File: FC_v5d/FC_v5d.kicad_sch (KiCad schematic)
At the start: 73 parts, among them IC3 RV-3028-C7_32.768kHz_1ppm_TA_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, J1 Conn_01x02, J12 USB_C_Receptacle_USB2.0_16P, J16 DEBUG, J18 Payload, J22 SWD Port, J3 Life Makes Lemonade, J5 BM04B-SRSS-TB(LF)(SN), J6 Conn_Coaxial, SW1 KMR2, SW2 KMR2, U12 TCA9548ARGERQ1, U14 TCA4307DGKR, U2 ZDSD04GLGEAG, U30 E28-2G4M27S, U4 RFM98PW, U7 LSM6DSOTR, U8 LSM303AGRTR

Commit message: Added XTSD Decoupling Cap
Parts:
- added C28: 100nf, Capacitor_SMD:C_0402_1005Metric, symbol Adafruit ItsyBitsy RP2040-eagle-import:CAP_CERAMIC_0402NO
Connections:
- net +3V3: now also C28.1
- net GND: now also C28.2
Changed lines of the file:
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@@
 	)
 	(junction
+		(at 64.77 222.25)
+		(diameter 0)
+		(color 0 0 0 0)
+	)
+	(junction
 		(at 237.49 125.73)
 		(diameter 0)
@@
 	(wire
 		(pts
+			(xy 64.77 222.25) (xy 71.12 222.25)
+		)
+		(stroke
+			(width 0)
+			(type default)
+		)
+	)
+	(wire
+		(pts
 			(xy 220.98 250.19) (xy 223.52 250.19)
 		)
@@
 	(wire
 		(pts
+			(xy 64.77 222.25) (xy 64.77 236.22)
+		)
+		(stroke
+			(width 0)
+			(type default)
+		)
+	)
+	(wire
+		(pts
 			(xy 397.002 44.45) (xy 397.002 29.591)
 		)
@@
 	(wire
 		(pts
+			(xy 71.12 222.25) (xy 71.12 226.06)
+		)
+		(stroke
+			(width 0)
+			(type default)
+		)
+	)
+	(wire
+		(pts
 			(xy 27.94 238.76) (xy 31.75 238.76)
 		)
@@
 	(wire
 		(pts
-			(xy 64.77 222.25) (xy 64.77 236.22)
-		)
-		(stroke
-			(width 0)
-			(type default)
-		)
-	)
-	(wire
-		(pts
 			(xy 163.83 232.41) (xy 166.37 232.41)
 		)
@@
 	)
 	(symbol
+		(lib_id "power:GND")
+		(at 71.12 233.68 0)
+		(unit 1)
+		(exclude_from_sim no)
+		(in_bom yes)
+		(on_board yes)
+		(dnp no)
+		(fields_autoplaced yes)
+		(property "Reference" "#PWR056"
+			(at 71.12 240.03 0)
+			(effects
+				(font
+					(size 1.27 1.27)
+				)
+				(hide yes)
+			)
+		)
+		(property "Value" "GND"
+			(at 71.12 238.1234 0)
+			(effects
+				(font
+					(size 1.27 1.27)
+				)
+			)
+		)
+		(property "Footprint" ""
+			(at 71.12 233.68 0)
+			(effects
+				(font
+					(size 1.27 1.27)
+				)
+				(hide yes)
+			)
+		)
+		(property "Datasheet" ""
+			(at 71.12 233.68 0)
+			(effects
+				(font
+					(size 1.27 1.27)
+				)
+				(hide yes)
+			)
+		)
+		(property "Description" ""
+			(at 71.12 233.68 0)
+			(effects
+				(font
+					(size 1.27 1.27)
+				)
+				(hide yes)
+			)
+		)
+		(pin "1"
+		)
+		(instances
+			(project "FC_v5d"
+				(path "/c64c0d72-a9f6-4f3a-891e-1f647558f538"
+					(reference "#PWR056")
+					(unit 1)
+				)
+			)
+		)
+	)
+	(symbol
 		(lib_id "Adafruit ItsyBitsy RP2040-eagle-import:SWITCH_TACT_SMT4.6X2.8")
 		(at 36.83 57.15 270)
@@
 					(unit 1)
 				)
+			)
+		)
+	)
+	(symbol
+		(lib_id "Adafruit ItsyBitsy RP2040-eagle-import:CAP_CERAMIC_0402NO")
+		(at 71.12 231.14 0)
+		(unit 1)
+		(exclude_from_sim no)
+		(in_bom yes)
+		(on_board yes)
+		(dnp no)
+		(property "Reference" "C28"
+			(at 68.83 229.89 90)
+			(effects
+				(font
+					(size 1.27 1.27)
+				)
+			)
+		)
+		(property "Value" "100nf"
+			(at 73.42 229.89 90)
+			(effects
+				(font
+					(size 1.27 1.27)
+				)
+			)
+		)
+		(property "Footprint" "Capacitor_SMD:C_0402_1005Metric"
+			(at 71.12 231.14 0)
+			(effects
+				(font
+					(size 1.27 1.27)
+				)
+				(hide yes)
+			)
+		)
+		(property "Datasheet" ""
+			(at 71.12 231.14 0)
+			(effects
+				(font
+					(size 1.27 1.27)
+				)
+				(hide yes)
+			)
+		)
+		(property "Description" ""
+			(at 71.12 231.14 0)
+			(effects
+				(font
+					(size 1.27 1.27)
+				)
+				(hide yes)
+			)
+		)
+		(pin "1"
+		)
+		(pin "2"
+		)
+		(instances
+			(project "FC_v5d"
+				(path "/c64c0d72-a9f6-4f3a-891e-1f647558f538"
+					(reference "C28")
+					(unit 1)
+				)

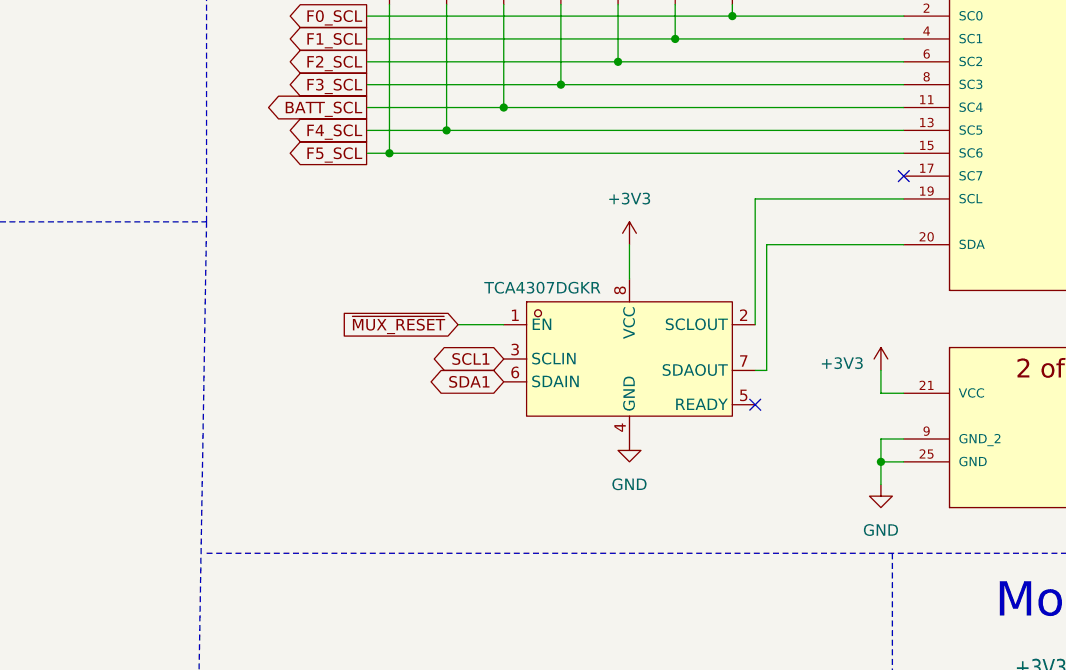
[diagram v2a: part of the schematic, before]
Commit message: Added Missing TCA4307 Pull Ups
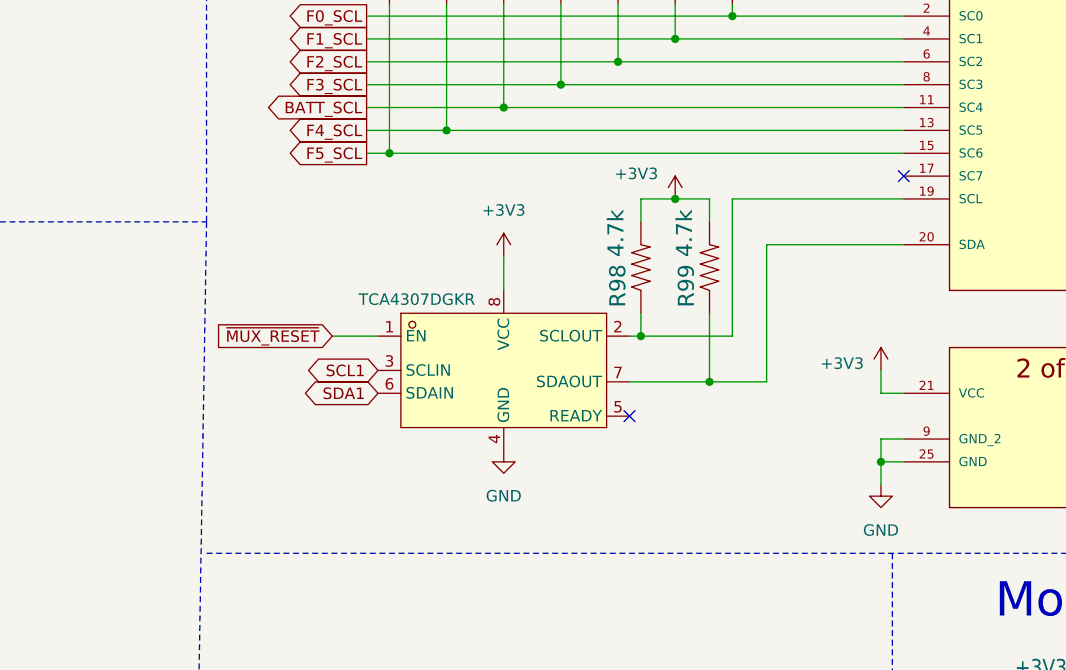
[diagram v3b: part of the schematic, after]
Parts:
- added R98, R99: 4.7k, Resistor_SMD:R_0603_1608Metric, symbol mainboard:RESISTOR0603
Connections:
- net +3V3: now also R98.2, R99.2
- net at U12.19 (SCL), U14.2 (SCLOUT): now also R98.1
- net at U12.20 (SDA), U14.7 (SDAOUT): now also R99.1

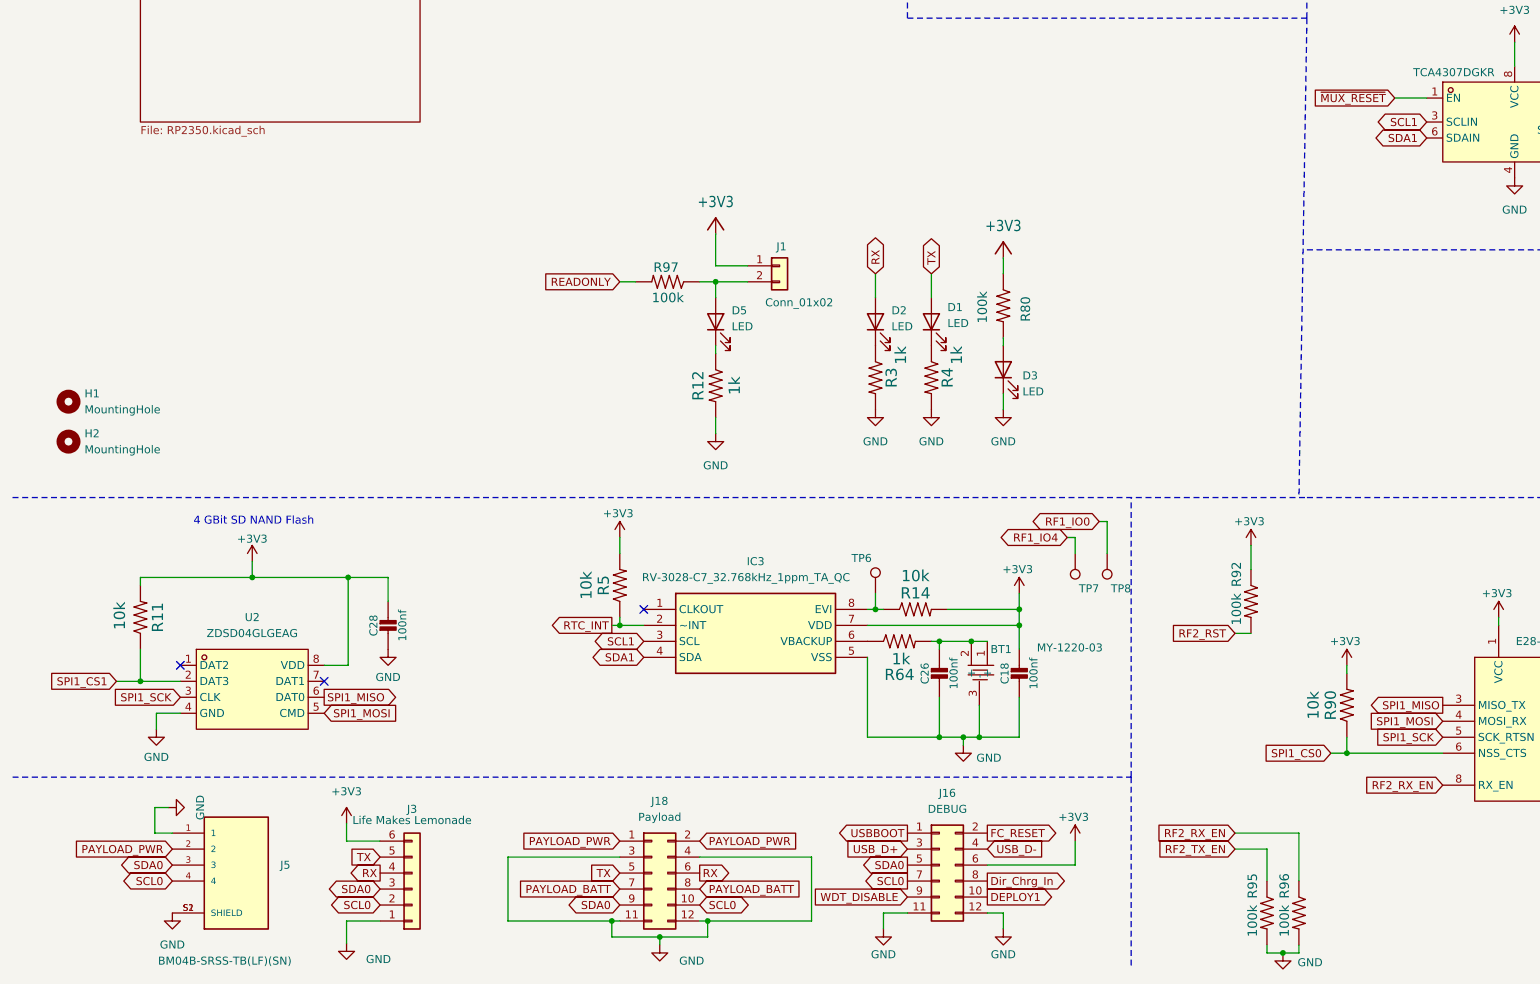
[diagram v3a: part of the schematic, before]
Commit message: Moved SDA0 and SCL0 to GP24 and GP25
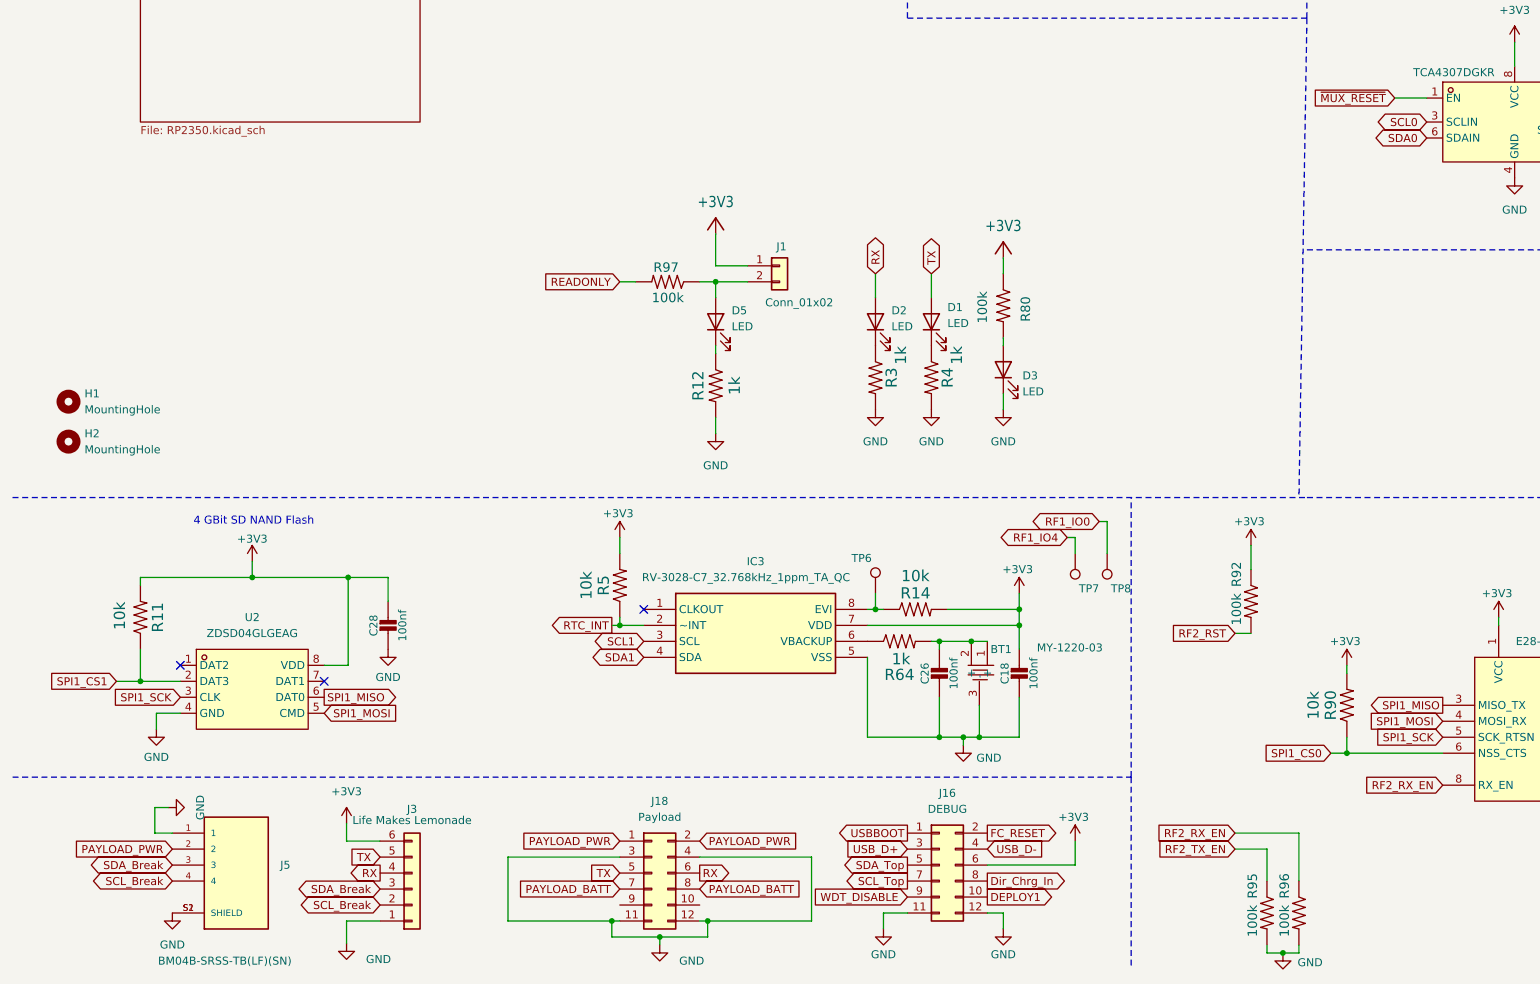
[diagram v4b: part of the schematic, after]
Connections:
- net SCL0: now also U14.3 (SCLIN); no longer J16.7 (Pin_7), J18.10 (Pin_10), J3.2 (Pin_2), J5.4
- net SCL1: no longer U14.3 (SCLIN)
- net SDA0: now also U14.6 (SDAIN); no longer J16.5 (Pin_5), J18.9 (Pin_9), J3.3 (Pin_3), J5.3
- net SDA1: no longer U14.6 (SDAIN)
- new net SCL_Break: J3.2 (Pin_2), J5.4
- new net SCL_Top: J16.7 (Pin_7)
- new net SDA_Break: J3.3 (Pin_3), J5.3
- new net SDA_Top: J16.5 (Pin_5)
